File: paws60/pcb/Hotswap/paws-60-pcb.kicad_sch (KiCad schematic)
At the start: 20 parts, among them J1 JST SH 4-pin, J2 AVR-ISP-6, SW1 Reset, U1 SRV05-4, U2 ATmega32U4-AU, Y1 16MHz

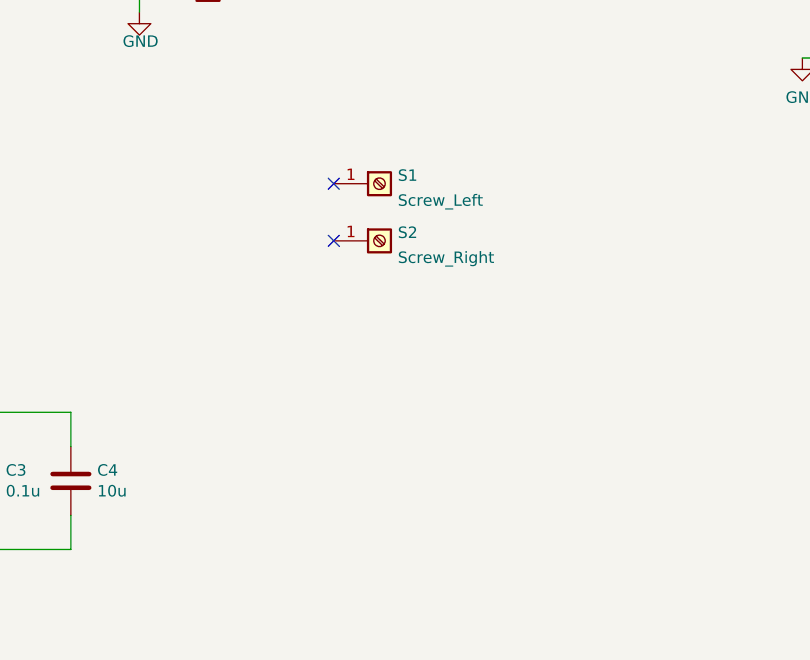
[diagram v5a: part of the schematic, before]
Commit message: Update changed for paws60
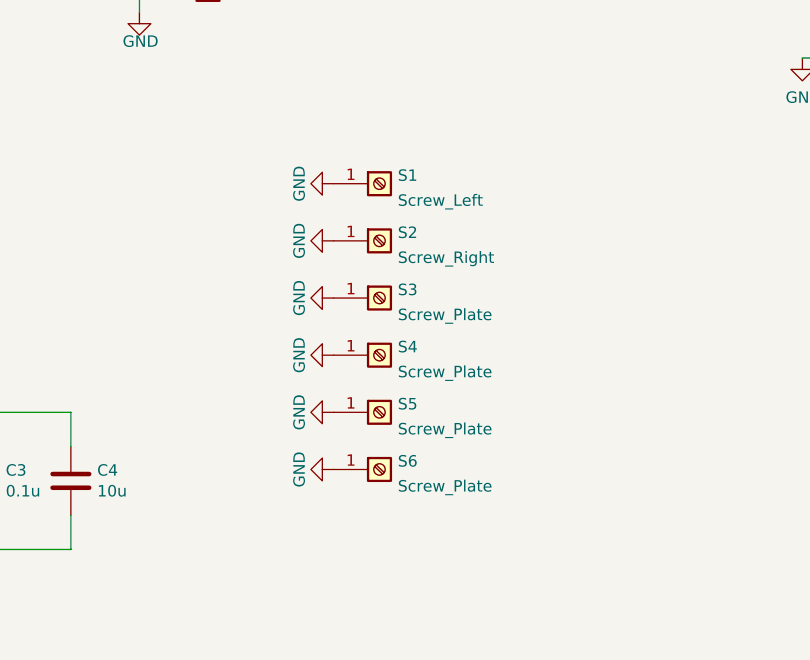
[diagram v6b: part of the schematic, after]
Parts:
- added S3, S4, S5, S6: Screw_Plate, Type-C:5.5_5x2.5mm, symbol Connector:Screw_Terminal_01x01
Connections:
- net GND: now also S1.1 (Pin_1), S2.1 (Pin_1), S3.1 (Pin_1), S4.1 (Pin_1), S5.1 (Pin_1), S6.1 (Pin_1)
- no-connect marks 7 -> 5
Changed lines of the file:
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@@
     (comment 2 "MIT License")
   )
-  (junction (at 60.96 177.8) (diameter 0) (color 0 0 0 0))
-  (junction (at 135.89 133.35) (diameter 0) (color 0 0 0 0))
-  (junction (at 123.19 142.24) (diameter 0) (color 0 0 0 0))
-  (junction (at 130.81 166.37) (diameter 0) (color 0 0 0 0))
   (junction (at 127 88.9) (diameter 0) (color 0 0 0 0))
-  (junction (at 106.68 88.9) (diameter 0) (color 0 0 0 0))
-  (junction (at 127 104.14) (diameter 0) (color 0 0 0 0))
-  (junction (at 116.84 104.14) (diameter 0) (color 0 0 0 0))
-  (junction (at 106.68 104.14) (diameter 0) (color 0 0 0 0))
+  (junction (at 116.84 88.9) (diameter 0) (color 0 0 0 0))
   (junction (at 63.5 83.82) (diameter 0) (color 0 0 0 0))
   (junction (at 123.19 125.73) (diameter 0) (color 0 0 0 0))
+  (junction (at 60.96 177.8) (diameter 0) (color 0 0 0 0))
+  (junction (at 130.81 166.37) (diameter 0) (color 0 0 0 0))
+  (junction (at 123.19 142.24) (diameter 0) (color 0 0 0 0))
+  (junction (at 116.84 104.14) (diameter 0) (color 0 0 0 0))
+  (junction (at 127 104.14) (diameter 0) (color 0 0 0 0))
+  (junction (at 106.68 104.14) (diameter 0) (color 0 0 0 0))
+  (junction (at 106.68 88.9) (diameter 0) (color 0 0 0 0))
   (junction (at 60.96 83.82) (diameter 0) (color 0 0 0 0))
-  (junction (at 116.84 88.9) (diameter 0) (color 0 0 0 0))
+  (junction (at 135.89 133.35) (diameter 0) (color 0 0 0 0))
   (no_connect (at 78.74 153.67))
   (no_connect (at 48.26 107.95))
   (no_connect (at 119.38 40.64))
-  (no_connect (at 166.37 69.85))
-  (no_connect (at 166.37 63.5))
   (no_connect (at 78.74 123.19))
   (no_connect (at 93.98 45.72))
@@
     (pin "1")
   )
+  (symbol (lib_id "power:GND") (at 166.37 63.5 270) (unit 1)
+    (in_bom yes) (on_board yes)
+    (property "Reference" "#PWR0107" (id 0) (at 160.02 63.5 0)
+      (effects (font (size 1.27 1.27)) hide)
+    )
+    (property "Value" "GND" (id 1) (at 162.56 63.5 0))
+    (property "Footprint" "" (id 2) (at 166.37 63.5 0)
+      (effects (font (size 1.27 1.27)) hide)
+    )
+    (property "Datasheet" "" (id 3) (at 166.37 63.5 0)
+      (effects (font (size 1.27 1.27)) hide)
+    )
+    (pin "1")
+  )
+  (symbol (lib_id "power:GND") (at 166.37 76.2 270) (unit 1)
+    (in_bom yes) (on_board yes)
+    (property "Reference" "#PWR0108" (id 0) (at 160.02 76.2 0)
+      (effects (font (size 1.27 1.27)) hide)
+    )
+    (property "Value" "GND" (id 1) (at 162.56 76.2 0))
+    (property "Footprint" "" (id 2) (at 166.37 76.2 0)
+      (effects (font (size 1.27 1.27)) hide)
+    )
+    (property "Datasheet" "" (id 3) (at 166.37 76.2 0)
+      (effects (font (size 1.27 1.27)) hide)
+    )
+    (pin "1")
+  )
+  (symbol (lib_id "power:GND") (at 166.37 82.55 270) (unit 1)
+    (in_bom yes) (on_board yes)
+    (property "Reference" "#PWR0103" (id 0) (at 160.02 82.55 0)
+      (effects (font (size 1.27 1.27)) hide)
+    )
+    (property "Value" "GND" (id 1) (at 162.56 82.55 0))
+    (property "Footprint" "" (id 2) (at 166.37 82.55 0)
+      (effects (font (size 1.27 1.27)) hide)
+    )
+    (property "Datasheet" "" (id 3) (at 166.37 82.55 0)
+      (effects (font (size 1.27 1.27)) hide)
+    )
+    (pin "1")
+  )
+  (symbol (lib_id "power:GND") (at 166.37 88.9 270) (unit 1)
+    (in_bom yes) (on_board yes)
+    (property "Reference" "#PWR0104" (id 0) (at 160.02 88.9 0)
+      (effects (font (size 1.27 1.27)) hide)
+    )
+    (property "Value" "GND" (id 1) (at 162.56 88.9 0))
+    (property "Footprint" "" (id 2) (at 166.37 88.9 0)
+      (effects (font (size 1.27 1.27)) hide)
+    )
+    (property "Datasheet" "" (id 3) (at 166.37 88.9 0)
+      (effects (font (size 1.27 1.27)) hide)
+    )
+    (pin "1")
+  )
+  (symbol (lib_id "Connector:Screw_Terminal_01x01") (at 171.45 95.25 0) (unit 1)
+    (in_bom yes) (on_board yes) (fields_autoplaced)
+    (property "Reference" "S6" (id 0) (at 173.482 94.3415 0)
+      (effects (font (size 1.27 1.27)) (justify left))
+    )
+    (property "Value" "Screw_Plate" (id 1) (at 173.482 97.1166 0)
+      (effects (font (size 1.27 1.27)) (justify left))
+    )
+    (property "Footprint" "Type-C:5.5_5x2.5mm" (id 2) (at 171.45 95.25 0)
+      (effects (font (size 1.27 1.27)) hide)
+    )
+    (property "Datasheet" "~" (id 3) (at 171.45 95.25 0)
+      (effects (font (size 1.27 1.27)) hide)
+    )
+    (pin "1")
+  )
+  (symbol (lib_id "Connector:Screw_Terminal_01x01") (at 171.45 82.55 0) (unit 1)
+    (in_bom yes) (on_board yes) (fields_autoplaced)
+    (property "Reference" "S4" (id 0) (at 173.482 81.6415 0)
+      (effects (font (size 1.27 1.27)) (justify left))
+    )
+    (property "Value" "Screw_Plate" (id 1) (at 173.482 84.4166 0)
+      (effects (font (size 1.27 1.27)) (justify left))
+    )
+    (property "Footprint" "Type-C:5.5_5x2.5mm" (id 2) (at 171.45 82.55 0)
+      (effects (font (size 1.27 1.27)) hide)
+    )
+    (property "Datasheet" "~" (id 3) (at 171.45 82.55 0)
+      (effects (font (size 1.27 1.27)) hide)
+    )
+    (pin "1")
+  )
+  (symbol (lib_id "Connector:Screw_Terminal_01x01") (at 171.45 88.9 0) (unit 1)
+    (in_bom yes) (on_board yes) (fields_autoplaced)
+    (property "Reference" "S5" (id 0) (at 173.482 87.9915 0)
+      (effects (font (size 1.27 1.27)) (justify left))
+    )
+    (property "Value" "Screw_Plate" (id 1) (at 173.482 90.7666 0)
+      (effects (font (size 1.27 1.27)) (justify left))
+    )
+    (property "Footprint" "Type-C:5.5_5x2.5mm" (id 2) (at 171.45 88.9 0)
+      (effects (font (size 1.27 1.27)) hide)
+    )
+    (property "Datasheet" "~" (id 3) (at 171.45 88.9 0)
+      (effects (font (size 1.27 1.27)) hide)
+    )
+    (pin "1")
+  )
   (symbol (lib_id "Connector:Screw_Terminal_01x01") (at 171.45 63.5 0) (unit 1)
     (in_bom yes) (on_board yes) (fields_autoplaced)
@@
     (pin "1")
   )
+  (symbol (lib_id "power:GND") (at 166.37 95.25 270) (unit 1)
+    (in_bom yes) (on_board yes)
+    (property "Reference" "#PWR0105" (id 0) (at 160.02 95.25 0)
+      (effects (font (size 1.27 1.27)) hide)
+    )
+    (property "Value" "GND" (id 1) (at 162.56 95.25 0))
+    (property "Footprint" "" (id 2) (at 166.37 95.25 0)
+      (effects (font (size 1.27 1.27)) hide)
+    )
+    (property "Datasheet" "" (id 3) (at 166.37 95.25 0)
+      (effects (font (size 1.27 1.27)) hide)
+    )
+    (pin "1")
+  )
   (symbol (lib_id "Connector:Screw_Terminal_01x01") (at 171.45 69.85 0) (unit 1)
     (in_bom yes) (on_board yes) (fields_autoplaced)
@@
     )
     (property "Datasheet" "~" (id 3) (at 171.45 69.85 0)
+      (effects (font (size 1.27 1.27)) hide)
+    )
+    (pin "1")
+  )
+  (symbol (lib_id "power:GND") (at 166.37 69.85 270) (unit 1)
+    (in_bom yes) (on_board yes)
+    (property "Reference" "#PWR0106" (id 0) (at 160.02 69.85 0)
+      (effects (font (size 1.27 1.27)) hide)
+    )
+    (property "Value" "GND" (id 1) (at 162.56 69.85 0))
+    (property "Footprint" "" (id 2) (at 166.37 69.85 0)
+      (effects (font (size 1.27 1.27)) hide)
+    )
+    (property "Datasheet" "" (id 3) (at 166.37 69.85 0)
+      (effects (font (size 1.27 1.27)) hide)
+    )
+    (pin "1")
+  )
+  (symbol (lib_id "Connector:Screw_Terminal_01x01") (at 171.45 76.2 0) (unit 1)
+    (in_bom yes) (on_board yes) (fields_autoplaced)
+    (property "Reference" "S3" (id 0) (at 173.482 75.2915 0)
+      (effects (font (size 1.27 1.27)) (justify left))
+    )
+    (property "Value" "Screw_Plate" (id 1) (at 173.482 78.0666 0)
+      (effects (font (size 1.27 1.27)) (justify left))
+    )
+    (property "Footprint" "Type-C:5.5_5x2.5mm" (id 2) (at 171.45 76.2 0)
+      (effects (font (size 1.27 1.27)) hide)
+    )
+    (property "Datasheet" "~" (id 3) (at 171.45 76.2 0)
       (effects (font (size 1.27 1.27)) hide)
     )
@@
       (reference "#PWR0102") (unit 1) (value "VBUS") (footprint "")
     )
+    (path "/43572087-2409-4d89-aee1-18574ef47490"
+      (reference "#PWR0103") (unit 1) (value "GND") (footprint "")
+    )
+    (path "/461b93ba-88ae-4363-bb1f-e1e0cd198f76"
+      (reference "#PWR0104") (unit 1) (value "GND") (footprint "")
+    )
+    (path "/afe4ddf5-c76d-4572-81d0-330059d750fb"
+      (reference "#PWR0105") (unit 1) (value "GND") (footprint "")
+    )
+    (path "/b477c692-d69e-492a-aa92-9273997954c7"
+      (reference "#PWR0106") (unit 1) (value "GND") (footprint "")
+    )
+    (path "/062f6c01-892e-4432-b018-78dd0c56a985"
+      (reference "#PWR0107") (unit 1) (value "GND") (footprint "")
+    )
+    (path "/3bc202e2-eb76-4a11-829b-88c32c2ac96b"
+      (reference "#PWR0108") (unit 1) (value "GND") (footprint "")
+    )
     (path "/00000000-0000-0000-0000-00005f24d3a7"
       (reference "C1") (unit 1) (value "0.1u") (footprint "Capacitor_SMD:C_0805_2012Metric")
@@
       (reference "S2") (unit 1) (value "Screw_Right") (footprint "Type-C:10x5_7x2.5mm")
     )
+    (path "/cacb411a-e977-4882-a6ae-7c4cc189ce96"
+      (reference "S3") (unit 1) (value "Screw_Plate") (footprint "Type-C:5.5_5x2.5mm")
+    )
+    (path "/4dbc1ec6-2f2b-4c9f-8993-aa0b492818dd"
+      (reference "S4") (unit 1) (value "Screw_Plate") (footprint "Type-C:5.5_5x2.5mm")
+    )
+    (path "/9cda4267-1d6b-4bec-9d19-2e8b11848744"
+      (reference "S5") (unit 1) (value "Screw_Plate") (footprint "Type-C:5.5_5x2.5mm")
+    )
+    (path "/47147ffa-2f90-4bfe-98b6-cfb93f1d46ab"
+      (reference "S6") (unit 1) (value "Screw_Plate") (footprint "Type-C:5.5_5x2.5mm")
+    )
     (path "/00000000-0000-0000-0000-00005f27b00d"
